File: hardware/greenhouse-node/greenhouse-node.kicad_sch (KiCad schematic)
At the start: 51 parts, among them J1 Conn_01x12_Male, J2 Conn_01x02_Male, J3 Conn_01x02_Male, J4 Conn_01x02_Male, J5 Conn_01x04_Male, J6 Conn_01x05_Female, U1 ATtiny84A-P, U2 L7805, U3 74HC595, Y1 8MHz

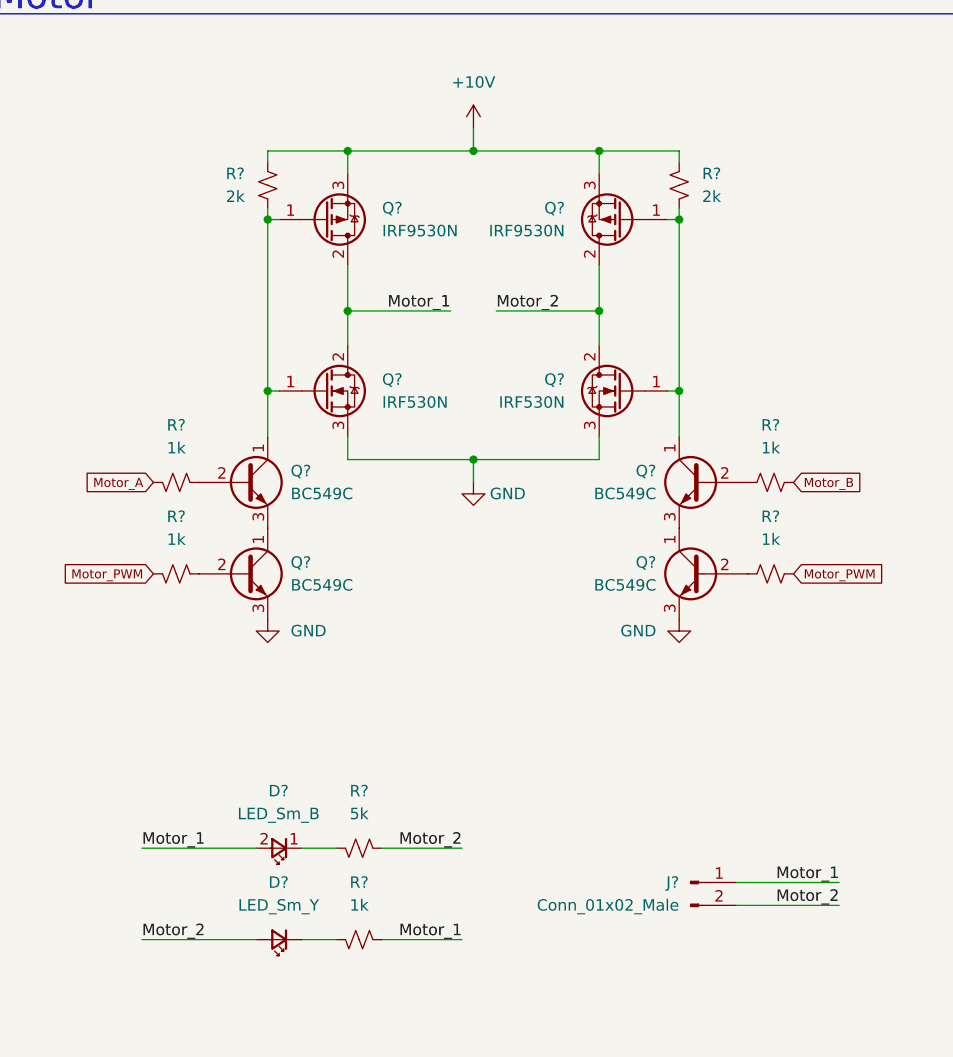
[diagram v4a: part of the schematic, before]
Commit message: Replace RX/TX modules with HC-12
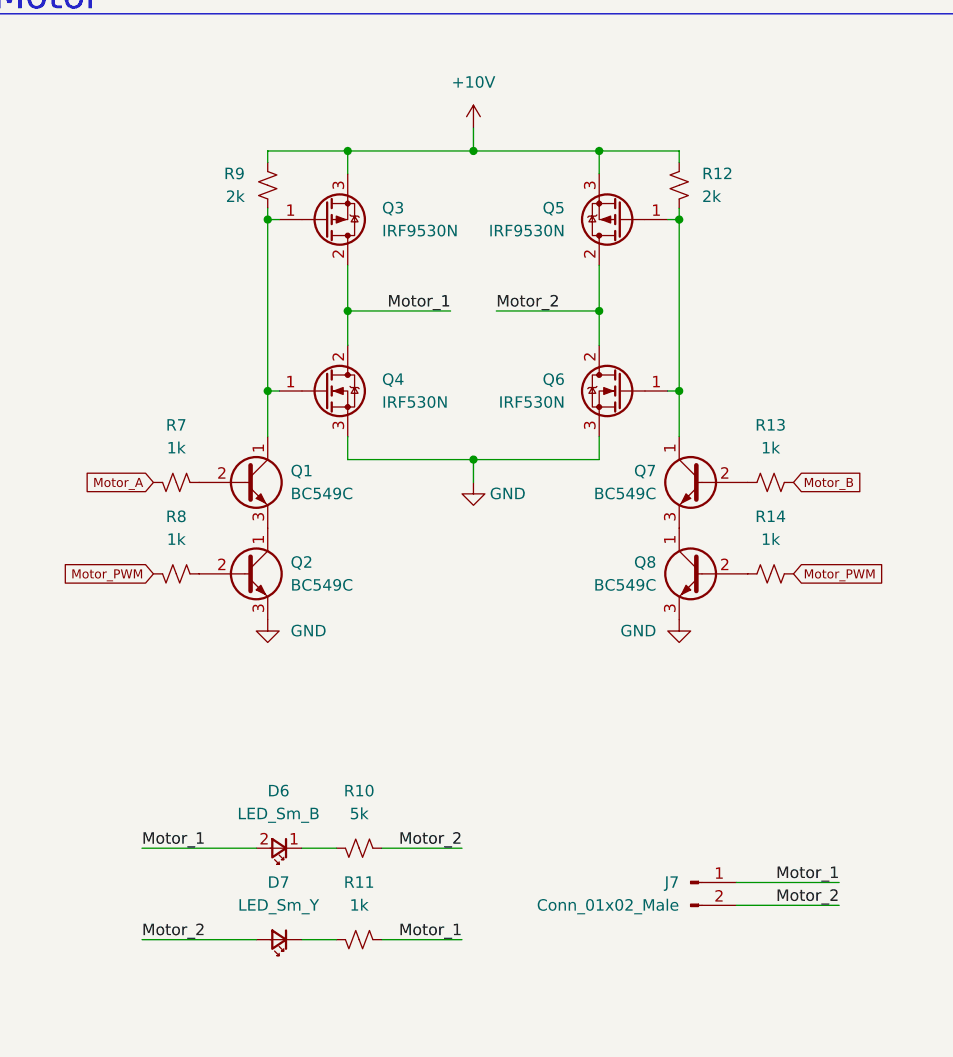
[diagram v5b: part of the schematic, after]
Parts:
- gave numbers to parts that had none: 19

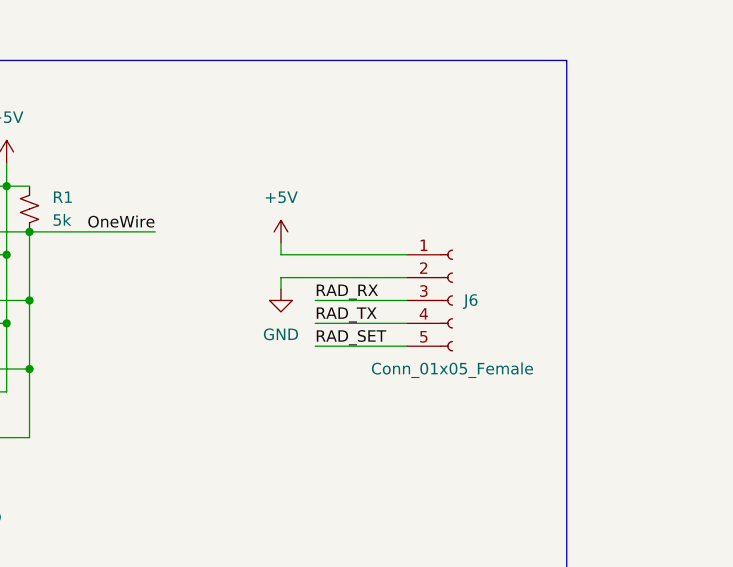
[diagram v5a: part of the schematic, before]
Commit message: Replace NodeMCU with Wemos D1
Also replaced SN74HC595 shift register with PCF8574AN
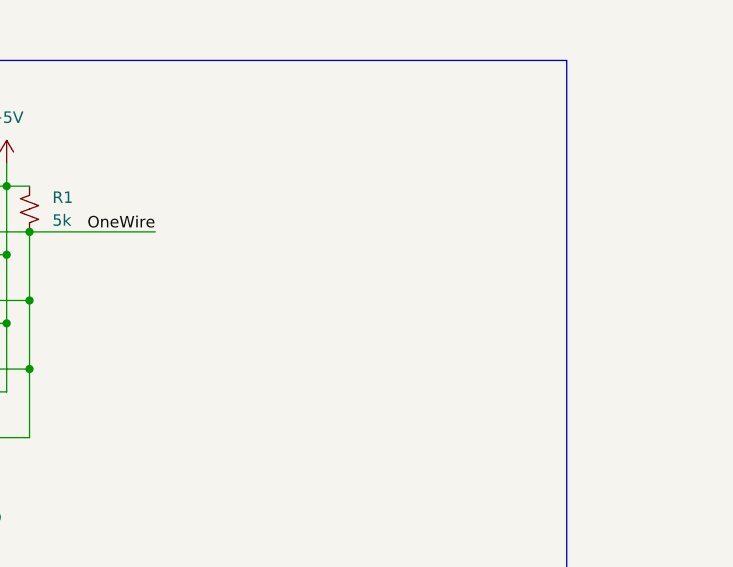
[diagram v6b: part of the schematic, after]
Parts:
- removed J6: Conn_01x05_Female, Connector_PinSocket_2.54mm:PinSocket_1x05_P2.54mm_Vertical, symbol Connector:Conn_01x05_Female
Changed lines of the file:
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@@
-    (stroke (width 0) (type default) (color 0 0 0 0))
-  )
-  (wire (pts (xy 289.56 59.69) (xy 275.59 59.69))
     (stroke (width 0) (type default) (color 0 0 0 0))
   )
@@
     (stroke (width 0) (type default) (color 0 0 0 0))
   )
-  (wire (pts (xy 275.59 55.88) (xy 275.59 57.15))
-    (stroke (width 0) (type default) (color 0 0 0 0))
-  )
   (wire (pts (xy 293.37 158.75) (xy 292.1 158.75))
     (stroke (width 0) (type default) (color 0 0 0 0))
@@
     (stroke (width 0) (type default) (color 0 0 0 0))
   )
-  (wire (pts (xy 275.59 59.69) (xy 275.59 60.96))
-    (stroke (width 0) (type default) (color 0 0 0 0))
-  )
   (wire (pts (xy 162.56 128.27) (xy 162.56 132.08))
     (stroke (width 0) (type default) (color 0 0 0 0))
   )
-  (wire (pts (xy 279.4 64.77) (xy 289.56 64.77))
-    (stroke (width 0) (type default) (color 0 0 0 0))
-  )
   (wire (pts (xy 92.71 146.05) (xy 96.52 146.05))
     (stroke (width 0) (type default) (color 0 0 0 0))
   )
-  (wire (pts (xy 275.59 57.15) (xy 289.56 57.15))
-    (stroke (width 0) (type default) (color 0 0 0 0))
-  )
   (wire (pts (xy 247.65 158.75) (xy 247.65 163.83))
     (stroke (width 0) (type default) (color 0 0 0 0))
@@
     (stroke (width 0) (type default) (color 0 0 0 0))
   )
-  (wire (pts (xy 279.4 67.31) (xy 289.56 67.31))
-    (stroke (width 0) (type default) (color 0 0 0 0))
-  )
   (wire (pts (xy 114.3 229.87) (xy 124.46 229.87))
     (stroke (width 0) (type default) (color 0 0 0 0))
@@
   )
   (wire (pts (xy 242.57 67.31) (xy 237.49 67.31))
-    (stroke (width 0) (type default) (color 0 0 0 0))
-  )
-  (wire (pts (xy 279.4 62.23) (xy 289.56 62.23))
     (stroke (width 0) (type default) (color 0 0 0 0))
   )
@@
     (effects (font (size 1.27 1.27)) (justify left bottom))
   )
-  (label "RAD_TX" (at 279.4 64.77 0)
-    (effects (font (size 1.27 1.27)) (justify left bottom))
-  )
   (label "SR_RCLK" (at 140.97 153.67 0)
     (effects (font (size 1.27 1.27)) (justify left bottom))
@@
     (effects (font (size 1.27 1.27)) (justify right bottom))
   )
-  (label "RAD_RX" (at 279.4 62.23 0)
-    (effects (font (size 1.27 1.27)) (justify left bottom))
-  )
   (label "XTAL2" (at 125.73 212.09 0)
     (effects (font (size 1.27 1.27)) (justify left bottom))
@@
   (label "SR_SER" (at 133.35 171.45 180)
     (effects (font (size 1.27 1.27)) (justify right bottom))
-  )
-  (label "RAD_SET" (at 279.4 67.31 0)
-    (effects (font (size 1.27 1.27)) (justify left bottom))
   )
   (label "OneWire" (at 133.35 163.83 180)
@@
     (pin "1")
   )
-  (symbol (lib_id "power:GND") (at 275.59 60.96 0) (unit 1)
-    (in_bom yes) (on_board yes) (fields_autoplaced)
-    (property "Reference" "#PWR022" (id 0) (at 275.59 67.31 0)
-      (effects (font (size 1.27 1.27)) hide)
-    )
-    (property "Value" "GND" (id 1) (at 275.59 66.04 0))
-    (property "Footprint" "" (id 2) (at 275.59 60.96 0)
-      (effects (font (size 1.27 1.27)) hide)
-    )
-    (property "Datasheet" "" (id 3) (at 275.59 60.96 0)
-      (effects (font (size 1.27 1.27)) hide)
-    )
-    (pin "1")
-  )
   (symbol (lib_id "Device:C_Small") (at 90.17 135.89 270) (unit 1)
     (in_bom yes) (on_board yes)
@@
     (pin "2")
   )
-  (symbol (lib_id "Connector:Conn_01x05_Female") (at 294.64 62.23 0) (unit 1)
-    (in_bom yes) (on_board yes) (fields_autoplaced)
-    (property "Reference" "J6" (id 0) (at 295.91 62.2299 0)
-      (effects (font (size 1.27 1.27)) (justify left))
-    )
-    (property "Value" "Conn_01x05_Female" (id 1) (at 294.64 69.85 0))
-    (property "Footprint" "Connector_PinSocket_2.54mm:PinSocket_1x05_P2.54mm_Vertical" (id 2) (at 294.64 62.23 0)
-      (effects (font (size 1.27 1.27)) hide)
-    )
-    (property "Datasheet" "~" (id 3) (at 294.64 62.23 0)
-      (effects (font (size 1.27 1.27)) hide)
-    )
-    (pin "1")
-    (pin "2")
-    (pin "3")
-    (pin "4")
-    (pin "5")
-  )
   (symbol (lib_id "Mechanical:MountingHole") (at 279.4 271.78 0) (unit 1)
     (in_bom yes) (on_board yes) (fields_autoplaced)
@@
     (pin "1")
     (pin "2")
-  )
-  (symbol (lib_id "power:+5V") (at 275.59 55.88 0) (mirror y) (unit 1)
-    (in_bom yes) (on_board yes) (fields_autoplaced)
-    (property "Reference" "#PWR0103" (id 0) (at 275.59 59.69 0)
-      (effects (font (size 1.27 1.27)) hide)
-    )
-    (property "Value" "+5V" (id 1) (at 275.59 50.8 0))
-    (property "Footprint" "" (id 2) (at 275.59 55.88 0)
-      (effects (font (size 1.27 1.27)) hide)
-    )
-    (property "Datasheet" "" (id 3) (at 275.59 55.88 0)
-      (effects (font (size 1.27 1.27)) hide)
-    )
-    (pin "1")
   )
   (symbol (lib_id "power:+10V") (at 270.51 129.54 0) (unit 1)
@@
       (reference "#PWR019") (unit 1) (value "GND") (footprint "")
     )
-    (path "/5c9a0412-4fb3-44e0-8564-dd1f1d19974f"
-      (reference "#PWR022") (unit 1) (value "GND") (footprint "")
-    )
     (path "/23b24f1a-0314-4640-ad02-55d3e4d235a9"
       (reference "#PWR0101") (unit 1) (value "GND") (footprint "")
@@
       (reference "#PWR0102") (unit 1) (value "+5V") (footprint "")
     )
-    (path "/888dc1b8-f3e3-43b5-bf21-93950079d164"
-      (reference "#PWR0103") (unit 1) (value "+5V") (footprint "")
-    )
     (path "/891475a2-32b2-43ac-a859-139e8f0f66ca"
       (reference "#PWR0104") (unit 1) (value "+10V") (footprint "")
@@
       (reference "J5") (unit 1) (value "Conn_01x04_Male") (footprint "Connector_JST:JST_XH_B4B-XH-A_1x04_P2.50mm_Vertical")
     )
-    (path "/6dcb6b48-87fc-45e5-b5d2-2e548601fab8"
-      (reference "J6") (unit 1) (value "Conn_01x05_Female") (footprint "Connector_PinSocket_2.54mm:PinSocket_1x05_P2.54mm_Vertical")
-    )
     (path "/bb0bf186-e26b-4d1b-9e6a-a6542e7c66a7"

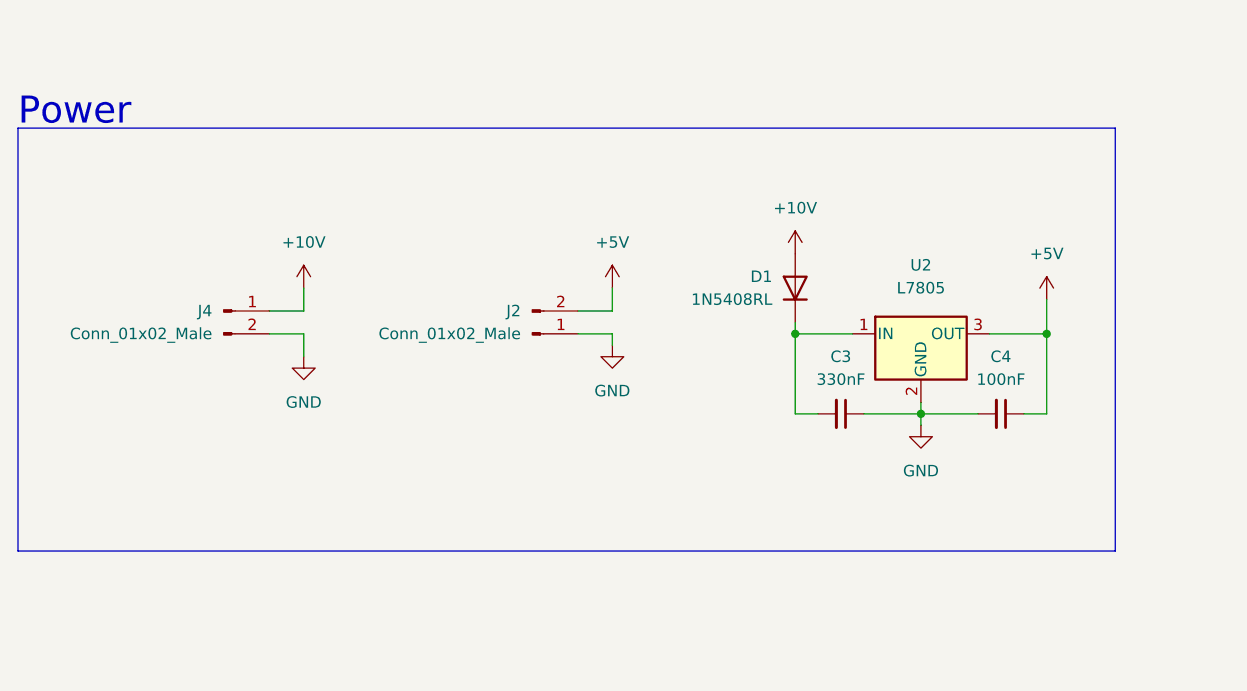
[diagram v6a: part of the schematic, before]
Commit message: Moved voltage drop to nodes
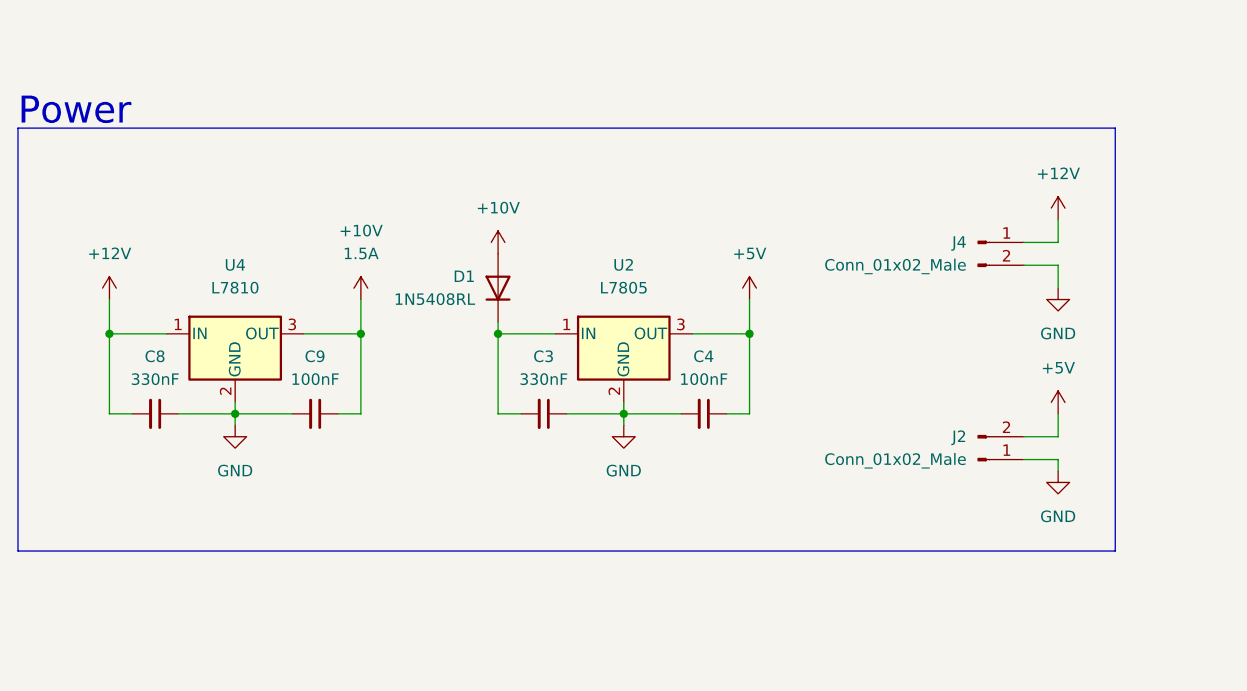
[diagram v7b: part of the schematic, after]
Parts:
- added C8: 330nF, Capacitor_THT:C_Disc_D4.7mm_W2.5mm_P5.00mm, symbol Device:C_Small
- added C9: 100nF, Capacitor_THT:C_Disc_D4.7mm_W2.5mm_P5.00mm, symbol Device:C_Small
- added U4: L7810, Package_TO_SOT_THT:TO-220-3_Vertical, symbol Regulator_Linear:L7805
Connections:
- net +10V: now also C9.1, U4.3 (OUT); no longer J4.1 (Pin_1)
- net GND: now also C8.1, C9.2, U4.2 (GND)
- new net +12V: C8.2, J4.1 (Pin_1), U4.1 (IN)
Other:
- moved on the sheet: C3, C4, D1, J2, J4, U2
